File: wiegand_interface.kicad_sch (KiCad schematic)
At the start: 14 parts, among them U10 EL3H7-G, U7 EL3H7-G, U8 EL3H7-G, U9 EL3H7-G

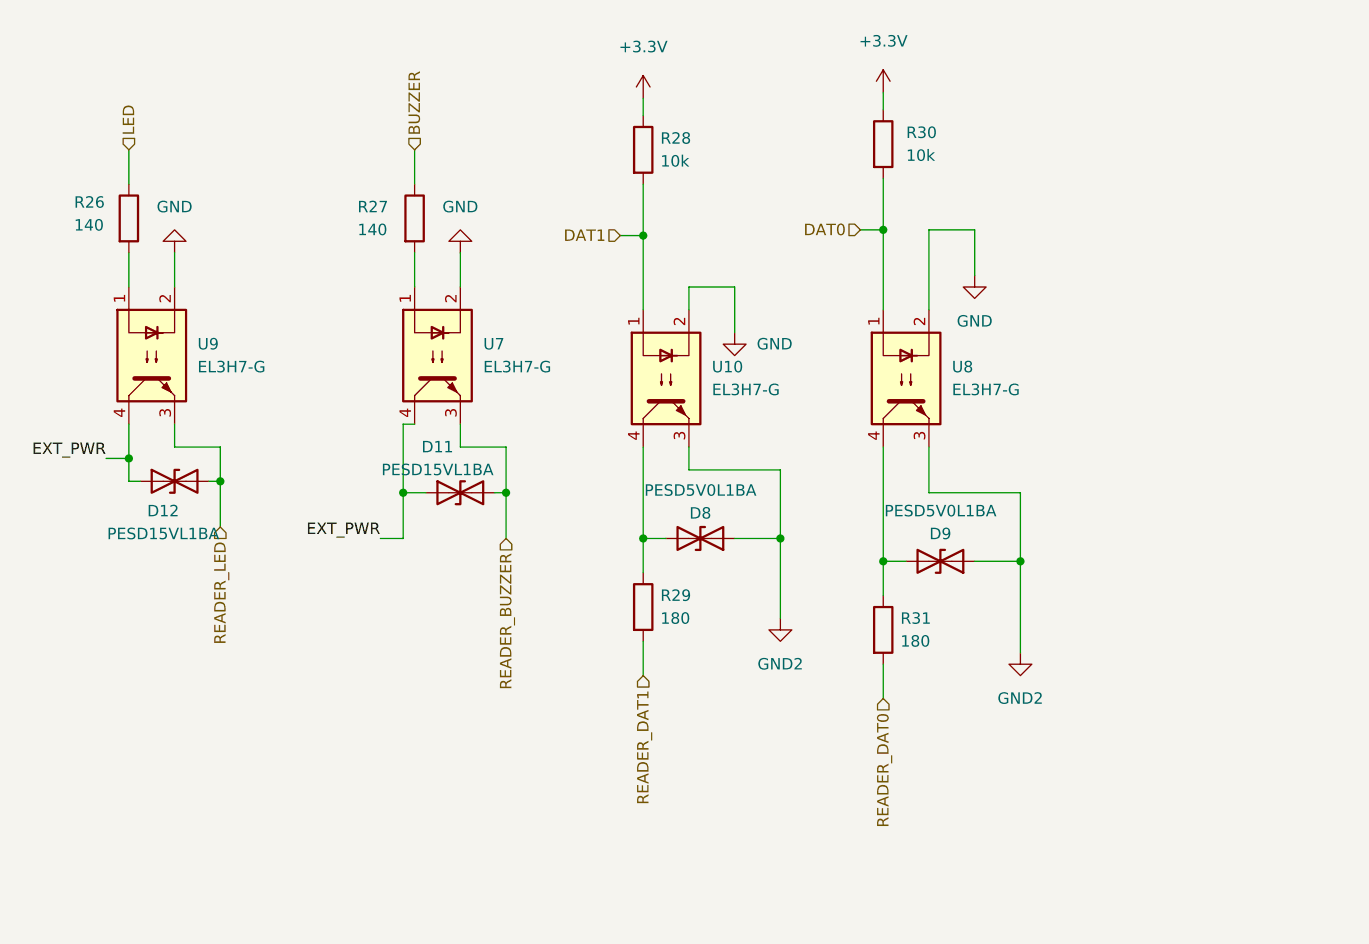
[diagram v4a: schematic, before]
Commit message: Prepare push in connectors, add aux input
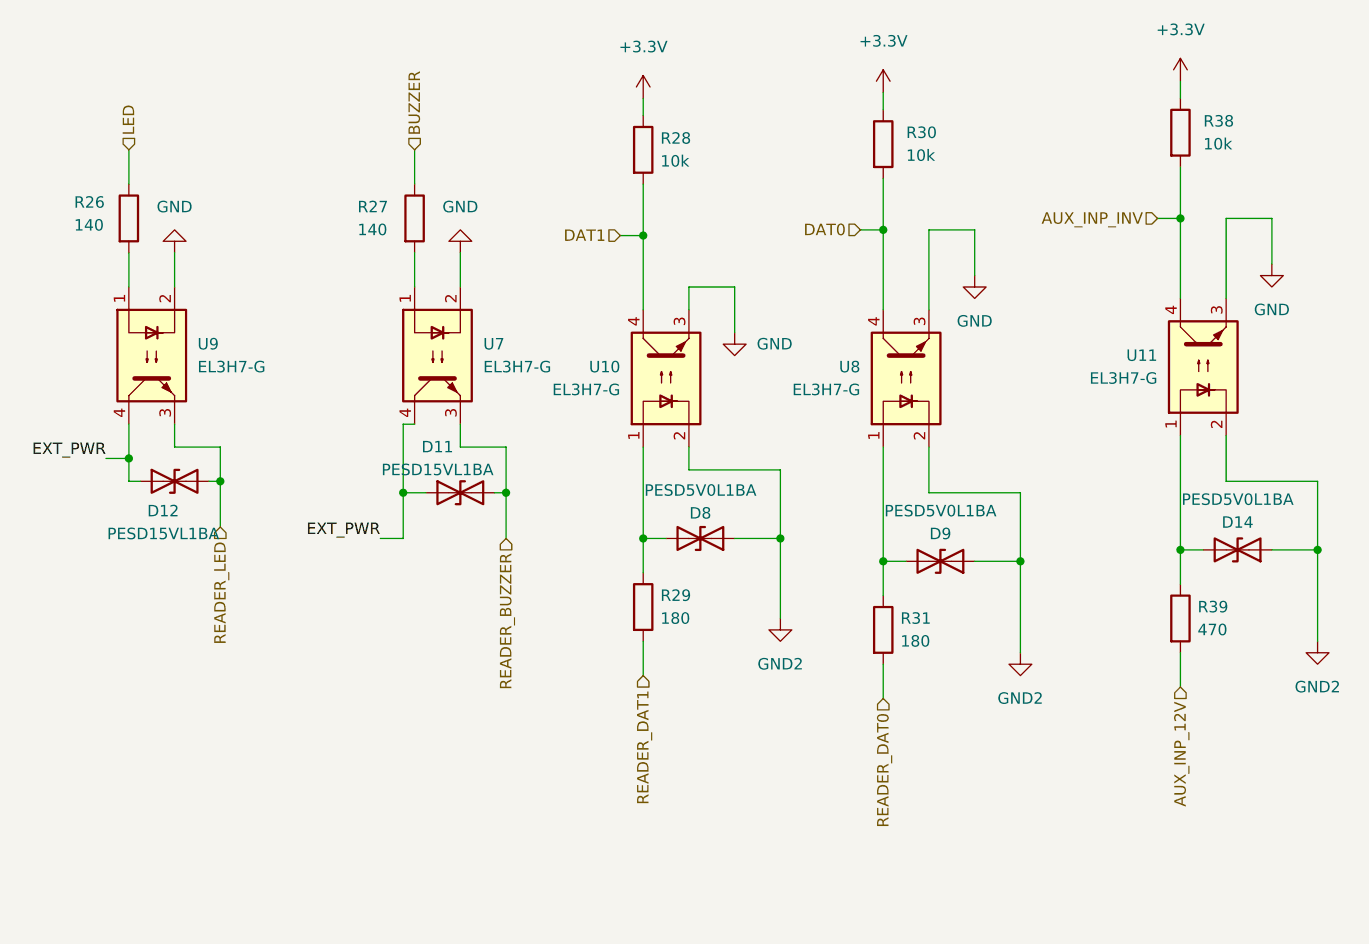
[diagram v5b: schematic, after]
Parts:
- added D14: PESD5V0L1BA, Diode_SMD:D_SOD-323, symbol Device:D_TVS
- added R38: 10k, Resistor_SMD:R_0603_1608Metric_Pad0.98x0.95mm_HandSolder, symbol Device:R
- added R39: 470, Resistor_SMD:R_0603_1608Metric_Pad0.98x0.95mm_HandSolder, symbol Device:R
- added U11: EL3H7-G, Package_SO:SSOP-4_4.4x2.6mm_P1.27mm, symbol Isolator:Optocoupler_DC_PhotoNPN_AKEC
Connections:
- net +3.3V: now also R38.1
- net DAT0: now also U8.4; no longer U8.1
- net DAT1: now also U10.4; no longer U10.1
- net GND: now also U10.3, U8.3, U11.3; no longer U10.2, U8.2
- net GND2: now also U10.2, U8.2, D14.1 (A1), U11.2; no longer U10.3, U8.3
- net at D9.2 (A2), R31.1: now also U8.1; no longer U8.4
- net at D8.2 (A2), R29.1: now also U10.1; no longer U10.4
- new net: D14.2 (A2), R39.1, U11.1
- new net AUX_INP_12V: R39.2
- new net AUX_INP_INV: R38.2, U11.4

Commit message: try playing around with the output screw terminals
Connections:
- net GND2: no longer D14.1 (A1), U11.2
- new net AUX_INP_GND: D14.1 (A1), U11.2
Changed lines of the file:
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@@
+	(wire
+		(pts
+			(xy 173.99 137.16) (xy 173.99 146.05)
+		)
+		(stroke
+			(width 0)
+			(type default)
+		)
+	)
 	(wire
 		(pts
@@
 	(wire
 		(pts
-			(xy 173.99 137.16) (xy 173.99 140.97)
-		)
-		(stroke
-			(width 0)
-			(type default)
-		)
-	)
-	(wire
-		(pts
 			(xy 173.99 125.73) (xy 176.53 125.73)
 		)
@@
 	(wire
 		(pts
-			(xy 189.23 125.73) (xy 189.23 135.89)
+			(xy 189.23 125.73) (xy 189.23 146.05)
 		)
 		(stroke
@@
 		)
 	)
-	(hierarchical_label "AUX_INP_12V"
+	(hierarchical_label "AUX_INP_GND"
 		(shape input)
-		(at 173.99 140.97 270)
+		(at 189.23 146.05 270)
 		(effects
 			(font
@@
 		(shape input)
 		(at 67.31 123.19 270)
+		(effects
+			(font
+				(size 1.27 1.27)
+			)
+			(justify right)
+		)
+	)
+	(hierarchical_label "AUX_INP_12V"
+		(shape input)
+		(at 173.99 146.05 270)
 		(effects
 			(font
@@
 					(unit 1)
 				)
-			)
-		)
-	)
-	(symbol
-		(lib_id "power:GND2")
-		(at 189.23 135.89 0)
-		(unit 1)
-		(exclude_from_sim no)
-		(in_bom yes)
-		(on_board yes)
-		(dnp no)
-		(fields_autoplaced yes)
-		(property "Reference" "#PWR085"
-			(at 189.23 142.24 0)
-			(effects
-				(font
-					(size 1.27 1.27)
-				)
-				(hide yes)
-			)
-		)
-		(property "Value" "GND2"
-			(at 189.23 140.97 0)
-			(effects
-				(font
-					(size 1.27 1.27)
-				)
-			)
-		)
-		(property "Footprint" ""
-			(at 189.23 135.89 0)
-			(effects
-				(font
-					(size 1.27 1.27)
-				)
-				(hide yes)
-			)
-		)
-		(property "Datasheet" ""
-			(at 189.23 135.89 0)
-			(effects
-				(font
-					(size 1.27 1.27)
-				)
-				(hide yes)
-			)
-		)
-		(property "Description" "Power symbol creates a global label with name \"GND2\" , ground"
-			(at 189.23 135.89 0)
-			(effects
-				(font
-					(size 1.27 1.27)
-				)
-				(hide yes)
-			)
-		)
-		(pin "1"
-		)
-		(instances
-			(project "Zamkonator"
-				(path "/727d6c0a-a0ef-4feb-9656-3db3cb90564a/6b89ba24-3094-438d-a07a-020a470fc0fc"
-					(reference "#PWR085")
-					(unit 1)
-				)

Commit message: Finish the schematic maybe
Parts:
- removed R28, R30, R38: 10k, Resistor_SMD:R_0603_1608Metric_Pad0.98x0.95mm_HandSolder, symbol Device:R
